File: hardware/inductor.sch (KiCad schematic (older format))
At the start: 10 parts, among them Q4 BC547

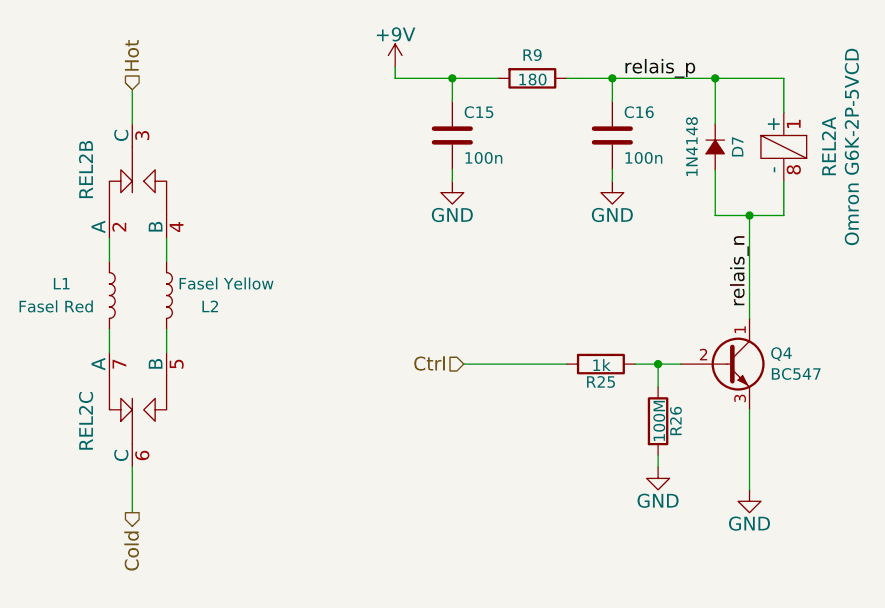
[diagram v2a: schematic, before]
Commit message: Fix relais supply
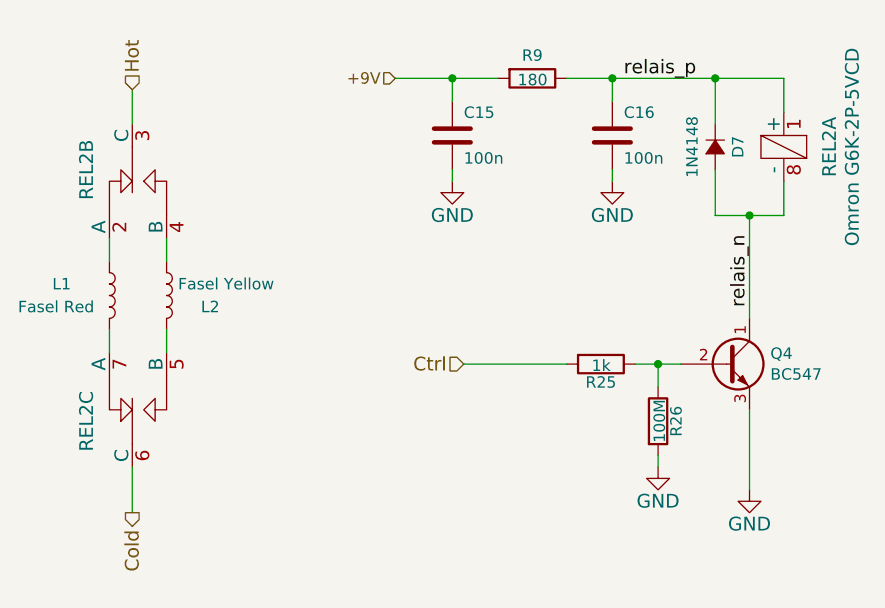
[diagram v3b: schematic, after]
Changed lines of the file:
@@
 	6450 2900 6450 2800
 Connection ~ 6450 2800
-$Comp
-L power:+9V #PWR?
-U 1 1 5CEC8AEA
-P 5500 2750
-AR Path="/56223A3E/5CEC8AEA" Ref="#PWR?"  Part="1"
-AR Path="/56223A52/54E9BE9F/5CEC8AEA" Ref="#PWR?"  Part="1"
-AR Path="/56223A60/54E9BE9F/5CEC8AEA" Ref="#PWR?"  Part="1"
-AR Path="/56223A6E/54E9BE9F/5CEC8AEA" Ref="#PWR?"  Part="1"
-AR Path="/56223A7C/54E9BE9F/5CEC8AEA" Ref="#PWR?"  Part="1"
-AR Path="/56223A90/54E9BE9F/5CEC8AEA" Ref="#PWR?"  Part="1"
-AR Path="/5CD91DFE/5CEC8AEA" Ref="#PWR?"  Part="1"
-AR Path="/5CE9535C/5CEC8AEA" Ref="#PWR0106"  Part="1"
-F 0 "#PWR0106" H 5500 2600 60  0001 C CNN
-F 1 "+9V" H 5500 2890 60  0000 C CNN
-F 2 "" H 5500 2750 60  0000 C CNN
-F 3 "" H 5500 2750 60  0000 C CNN
-	1    5500 2750
-	1    0    0    -1
-$EndComp
-Wire Wire Line
-	5500 2750 5500 2800
 Wire Wire Line
 	5750 3250 5750 3200
@@
 Wire Wire Line
 	4500 3500 4500 3600
+Text HLabel 5500 2800 0    50   Input ~ 0
++9V
 $EndSCHEMATC
